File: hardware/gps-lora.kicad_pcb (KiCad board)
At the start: 4 copper layers, 0 parts

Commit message: Complete schematic, place and partially route the PCB
Schematic:
- Add Storage & Display sheet (microSD, FH12 OLED connector, TLV75801
  3.8 V VBAT regulator, charge-pump parts) and Radio sheet fixes
- Select remaining parts (PTS810, 1206L075THYR, SMF5.0A, MCP120 EN
  supervisor DNP, Elna DSK backup cap), add mounting holes and fiducials
- Pin changes for routability: PPS -> IO15, LoRa MOSI -> IO47,
  LoRa RESET -> IO48, LoRa DIO0 -> IO1
- Remove optional SPI clock filter parts (R309/C307, R310/C308)
- Remove company name from title blocks (personal project)

PCB (60 x 120 mm, 4 layers):
- Place all parts; GNSS zone with custom DRC rules (kicad_dru)
- Project ESP32-S3-WROOM-1 footprint with 0.4 mm thermal vias
- GND / +3V3 / +5V copper zones
- Route power path, GNSS, microSD and LoRa buses
- DRC clean except unrouted nets and expected silkscreen-at-edge items

Docs: selected-parts table, pin table and EMC deviation in PCB_DESIGN.md

Co-Authored-By: Claude Opus 5.5 <noreply@anthropic.com>
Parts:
- added C201: 4.7nF, Capacitor_SMD:C_0402_1005Metric, F.Cu at (78.8, 145.2)
- added C202: 2200uF, Capacitor_SMD:CP_Elec_10x10.5, F.Cu at (61.8, 118.5)
- added C203: 22uF, Capacitor_SMD:C_0805_2012Metric, F.Cu at (79.6, 141.0)
- added C204: 100nF, Capacitor_SMD:C_0402_1005Metric, F.Cu at (81.0, 143.0)
- added C205: 22uF, Capacitor_SMD:C_0805_2012Metric, F.Cu at (85.6, 141.0)
- added C206: 100nF, Capacitor_SMD:C_0402_1005Metric, F.Cu at (83.6, 143.0)
- added C301: 100uF, Capacitor_SMD:C_1210_3225Metric, F.Cu at (107.0, 123.4)
- added C302: 10uF, Capacitor_SMD:C_0805_2012Metric, F.Cu at (107.6, 126.6)
- added C303: 100nF, Capacitor_SMD:C_0402_1005Metric, F.Cu at (107.2, 128.8)
- added C304: 1uF, Capacitor_SMD:C_0402_1005Metric, F.Cu at (105.6, 128.8)
- added C305: DNP, Capacitor_SMD:C_0402_1005Metric, F.Cu at (92.0, 126.8)
- added C306: DNP, Capacitor_SMD:C_0402_1005Metric, F.Cu at (93.3, 126.8)
- added C401: 10uF, Capacitor_SMD:C_0805_2012Metric, F.Cu at (84.0, 50.2)
- added C402: 100nF, Capacitor_SMD:C_0402_1005Metric, F.Cu at (81.9, 50.9)
- added C404: 100uF, Capacitor_SMD:C_1210_3225Metric, F.Cu at (68.6, 109.2)
- added C405: 10uF, Capacitor_SMD:C_0805_2012Metric, F.Cu at (64.6, 108.6)
- added C406: 100nF, Capacitor_SMD:C_0402_1005Metric, F.Cu at (61.8, 108.4)
- added C501: 100uF, Capacitor_SMD:C_1210_3225Metric, F.Cu at (62.6, 126.2)
- added C502: 10uF, Capacitor_SMD:C_0805_2012Metric, F.Cu at (58.0, 128.4)
- added C503: 100nF, Capacitor_SMD:C_0402_1005Metric, F.Cu at (57.5, 130.9)
- added C504: 1uF, Capacitor_SMD:C_0402_1005Metric, F.Cu at (90.6, 126.3)
- added C505: 1uF, Capacitor_SMD:C_0402_1005Metric, F.Cu at (89.4, 126.3)
- added C506: 1uF, Capacitor_SMD:C_0402_1005Metric, F.Cu at (88.2, 126.3)
- added C507: 1uF, Capacitor_SMD:C_0402_1005Metric, F.Cu at (87.0, 126.3)
- added C508: 2.2uF, Capacitor_SMD:C_0603_1608Metric, F.Cu at (78.4, 126.3)
- added C509: 4.7uF, Capacitor_SMD:C_0603_1608Metric, F.Cu at (80.0, 126.3)
- added C510: 1uF, Capacitor_SMD:C_0402_1005Metric, F.Cu at (89.2, 129.0)
- added C511: 1uF, Capacitor_SMD:C_0402_1005Metric, F.Cu at (83.4, 129.1)
- added D201: SMF5.0A, Diode_SMD:D_SOD-123F, F.Cu at (75.5, 134.5)
- added D202: Schottky, Diode_SMD:D_SMA, F.Cu at (71.0, 130.6)
- added D301: Green, LED_SMD:LED_0603_1608Metric, F.Cu at (101.3, 126.3)
- added D401: BAT54, Diode_SMD:D_SOD-323, F.Cu at (71.5, 83.5)
- added F201: 0.75A PTC, Fuse:Fuse_1206_3216Metric, F.Cu at (75.5, 137.5)
- added FID1: Fiducial, Fiducial:Fiducial_1mm_Mask2mm, F.Cu at (72.0, 33.0)
- added FID2: Fiducial, Fiducial:Fiducial_1mm_Mask2mm, F.Cu at (107.0, 80.0)
- added FID3: Fiducial, Fiducial:Fiducial_1mm_Mask2mm, F.Cu at (53.0, 122.0)
- added H1: MountingHole_Pad, MountingHole:MountingHole_2.2mm_M2_Pad_Via, F.Cu at (53.5, 33.5)
- added H2: MountingHole_Pad, MountingHole:MountingHole_2.2mm_M2_Pad_Via, F.Cu at (106.5, 33.5)
- added H3: MountingHole_Pad, MountingHole:MountingHole_2.2mm_M2_Pad_Via, F.Cu at (53.5, 129.5)
- added H4: MountingHole_Pad, MountingHole:MountingHole_2.2mm_M2_Pad_Via, F.Cu at (82.5, 147.0)
- added J201: TYPE-C-31-M-12, Connector_USB:USB_C_Receptacle_HRO_TYPE-C-31-M-12, F.Cu at (72.4, 146.3)
- added J301: TC2030-NL, Connector:Tag-Connect_TC2030-IDC-NL_2x03_P1.27mm_Vertical, F.Cu at (101.5, 116.0)
- added J401: U.FL, Connector_Coaxial:U.FL_Hirose_U.FL-R-SMT-1_Vertical, F.Cu at (53.3, 110.0)
- added J501: DM3AT-SF-PEJM5, Connector_Card:microSD_HC_Hirose_DM3AT-SF-PEJM5, F.Cu at (59.0, 140.9)
- added J502: FH12-30S-0.5SH(55), Connector_FFC-FPC:Hirose_FH12-30S-0.5SH_1x30-1MP_P0.50mm_Horizontal, F.Cu at (86.5, 121.5)
- added R201: 5.1k, Resistor_SMD:R_0402_1005Metric, F.Cu at (69.0, 140.2)
- added R202: 5.1k, Resistor_SMD:R_0402_1005Metric, F.Cu at (75.0, 140.2)
- added R203: 1M, Resistor_SMD:R_0402_1005Metric, F.Cu at (78.8, 143.4)
- added R204: 0R, Resistor_SMD:R_0805_2012Metric, F.Cu at (76.3, 130.6)
- added R205: 10k, Resistor_SMD:R_0402_1005Metric, F.Cu at (100.6, 129.0)
- added R206: 15k, Resistor_SMD:R_0402_1005Metric, F.Cu at (101.9, 129.0)
- added R301: 10k, Resistor_SMD:R_0402_1005Metric, F.Cu at (104.4, 128.8)
- added R302: 10k, Resistor_SMD:R_0402_1005Metric, F.Cu at (94.6, 126.8)
- added R303: 1k, Resistor_SMD:R_0402_1005Metric, F.Cu at (99.7, 126.8)
- added R304: 0R, Resistor_SMD:R_0402_1005Metric, F.Cu at (92.0, 129.0)
- added R305: 0R, Resistor_SMD:R_0402_1005Metric, F.Cu at (93.3, 129.0)
- added R306: 499R, Resistor_SMD:R_0402_1005Metric, F.Cu at (99.0, 120.2)
- added R307: 100R, Resistor_SMD:R_0402_1005Metric, F.Cu at (97.1, 129.0)
- added R308: 100R, Resistor_SMD:R_0402_1005Metric, F.Cu at (95.8, 129.0)
- added R401: 1k, Resistor_SMD:R_0402_1005Metric, F.Cu at (71.5, 80.0)
- added R501: 47k, Resistor_SMD:R_0402_1005Metric, F.Cu at (59.5, 130.6)
- added R502: 47k, Resistor_SMD:R_0402_1005Metric, F.Cu at (60.8, 130.6)
- added R503: 47k, Resistor_SMD:R_0402_1005Metric, F.Cu at (62.1, 130.6)
- added R504: 47k, Resistor_SMD:R_0402_1005Metric, F.Cu at (63.4, 130.6)
- added R505: 10k, Resistor_SMD:R_0402_1005Metric, F.Cu at (85.8, 126.3)
- added R506: 4.7k, Resistor_SMD:R_0402_1005Metric, F.Cu at (84.6, 126.3)
- added R507: 4.7k, Resistor_SMD:R_0402_1005Metric, F.Cu at (83.4, 126.3)
- added R508: 390k, Resistor_SMD:R_0402_1005Metric, F.Cu at (81.6, 126.3)
- added R509: 59k, Resistor_SMD:R_0402_1005Metric, F.Cu at (82.2, 129.1)
- added R510: 10k, Resistor_SMD:R_0402_1005Metric, F.Cu at (81.0, 129.1)
- added SW301: RESET, Button_Switch_SMD:SW_SPST_PTS810, F.Cu at (106.5, 92.0)
- added SW302: BOOT, Button_Switch_SMD:SW_SPST_PTS810, F.Cu at (106.5, 99.0)
- added SW303: EJECT, Button_Switch_SMD:SW_SPST_PTS810, F.Cu at (106.5, 106.0)
- added TP201: TestPoint, TestPoint:TestPoint_Pad_D1.0mm, F.Cu at (68.5, 126.5)
- added TP202: TestPoint, TestPoint:TestPoint_Pad_D1.0mm, F.Cu at (71.0, 126.5)
- added TP203: TestPoint, TestPoint:TestPoint_Pad_D1.0mm, F.Cu at (73.5, 126.5)
- added TP204: TestPoint, TestPoint:TestPoint_Pad_D1.0mm, F.Cu at (76.0, 126.5)
- added TP401: SAFEBOOT, TestPoint:TestPoint_Pad_D1.0mm, F.Cu at (80.0, 79.6)
- added TP501: VBAT, TestPoint:TestPoint_Pad_D1.0mm, F.Cu at (79.4, 129.4)
- added U201: USBLC6-2SC6, Package_TO_SOT_SMD:SOT-23-6, F.Cu at (70.0, 137.5)
- added U202: AP7361C-33E, Package_TO_SOT_SMD:SOT-223-3_TabPin2, F.Cu at (82.5, 135.4)
- added U301: ESP32-S3-WROOM-1-N8, gps-lora:ESP32-S3-WROOM-1, F.Cu at (103.2, 140.0)
- added U302: MCP120T-300I/TT, Package_TO_SOT_SMD:SOT-23, F.Cu at (102.2, 122.0)
- added U401: SAM-M10Q, RF_GPS:ublox_SAM-M8Q, F.Cu at (80.0, 60.0)
- added U402: RFM95W-868S2, RF_Module:HOPERF_RFM9XW_SMD, F.Cu at (60.8, 98.0)
- added U501: TLV75801PDBV, Package_TO_SOT_SMD:SOT-23-5, F.Cu at (86.4, 129.1)
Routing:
- net GNSS_RESET_N: track 0.00 -> 107.6 mm, vias 0 -> 2
- net LORA_DIO0: track 0.00 -> 101.2 mm, vias 0 -> 4
- net +3V3: track 0.00 -> 99.6 mm, vias 0 -> 4
- net LORA_RESET: track 0.00 -> 86.9 mm, vias 0 -> 2
- net GNSS_PPS: track 0.00 -> 84.8 mm, vias 0 -> 2
- net LORA_DIO1: track 0.00 -> 83.4 mm, vias 0 -> 4
- net LORA_NSS: track 0.00 -> 82.3 mm, vias 0 -> 2
- net LORA_MOSI: track 0.00 -> 80.0 mm, vias 0 -> 2
- net GNSS_RXD: track 0.00 -> 77.9 mm, vias 0 -> 2
- net LORA_MISO: track 0.00 -> 77.2 mm, vias 0 -> 2
- net LORA_SCK: track 0.00 -> 77.0 mm, vias 0 -> 4
- net GNSS_TXD: track 0.00 -> 74.7 mm, vias 0 -> 2
- net SD_MISO: track 0.00 -> 57.8 mm, vias 0 -> 2
- net +5V: track 0.00 -> 56.9 mm, vias 0 -> 3
- net SD_CS: track 0.00 -> 43.7 mm, vias 0 -> 2
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- added copper zone on In2.Cu, net +3V3
- added copper zone on In2.Cu, net +5V
- added copper zone on B.Cu, net GND
- added copper zone on F.Cu, net GND
- added copper zone on In1.Cu, net GND
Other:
- board outline added: 60 x 120 mm
- board text added: "OLED PANEL - NO PARTS"

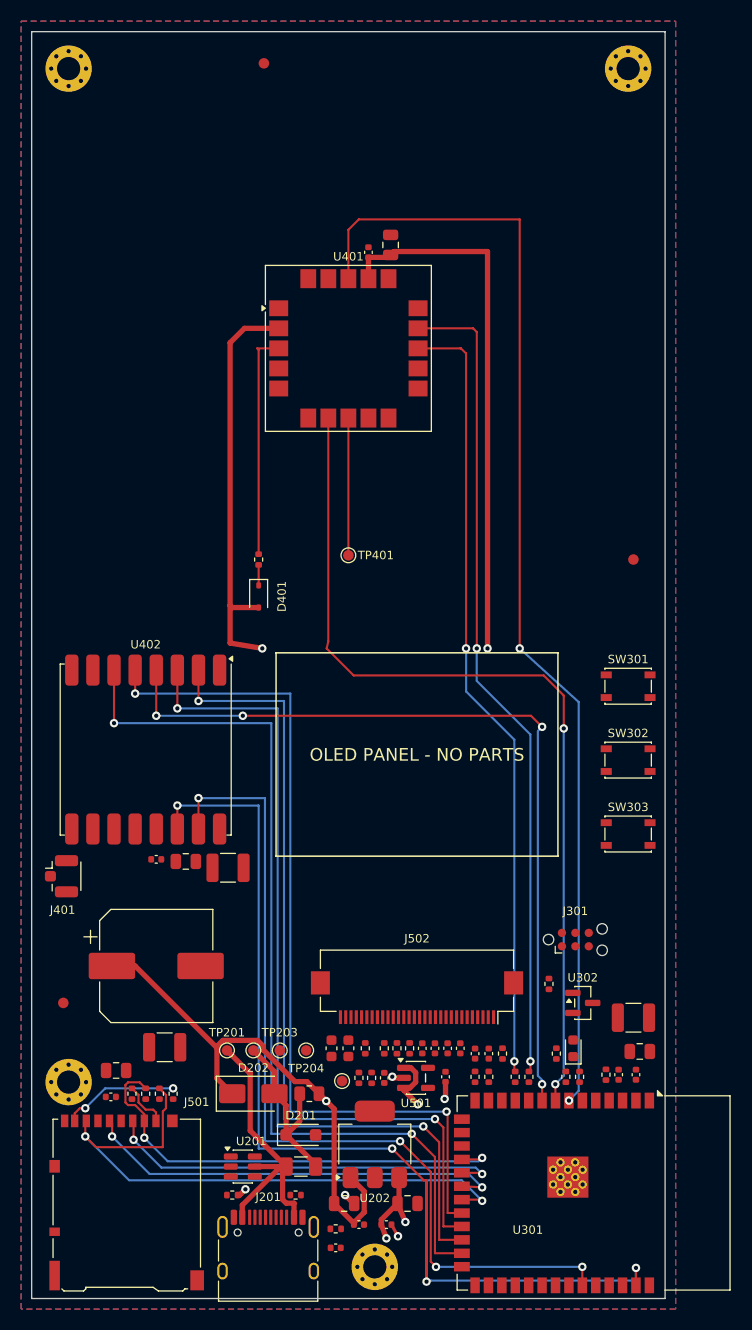
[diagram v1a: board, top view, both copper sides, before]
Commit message: Finish PCB routing, add BOM part numbers and fab export
Routing (DRC: 0 errors, 0 unconnected; ERC: 0)
- Complete the remaining nets on top of the GUI routing; GND stitching
  grid and edge fence; every GND pad reaches the L2 plane
- Re-lay the microSD bus under USB D+ so the USBLC6 and VBUS TVS get
  direct GND vias; lift LoRa NSS/MISO/MOSI to clear the TVS via
- Reroute D-, VBUS sense, CC2, BOOT, OLED SDA/SCL, LED and TXD0_R; remove
  vias in pads (R205, R505, R204, R507, U301 pin 7)
- Placement tweaks: C306 moved, C508/C509/R508 rotated 180, R302 moved
- PCB title block with rev v0.1

Parts and outputs
- MPN and Manufacturer fields on all placed parts (tools/add-mpn.py)
- tools/fab-export.py: ERC/DRC gate, zone refill, Gerbers, drill, BOM,
  pick-and-place and fab notes for Lion Circuits
- OLED panel DS501: schematic symbol and board-only 3D footprint
- Elna DSK footprint for C403 (not placed yet)
- kicad-routing skill under .claude/skills

Open before fab (see docs/PCB_DESIGN.md Open items): J502 pin order is
mirrored against the panel FPC; Lion stackup widths; C403 placement.

Co-Authored-By: Claude Opus 5.5 <noreply@anthropic.com>
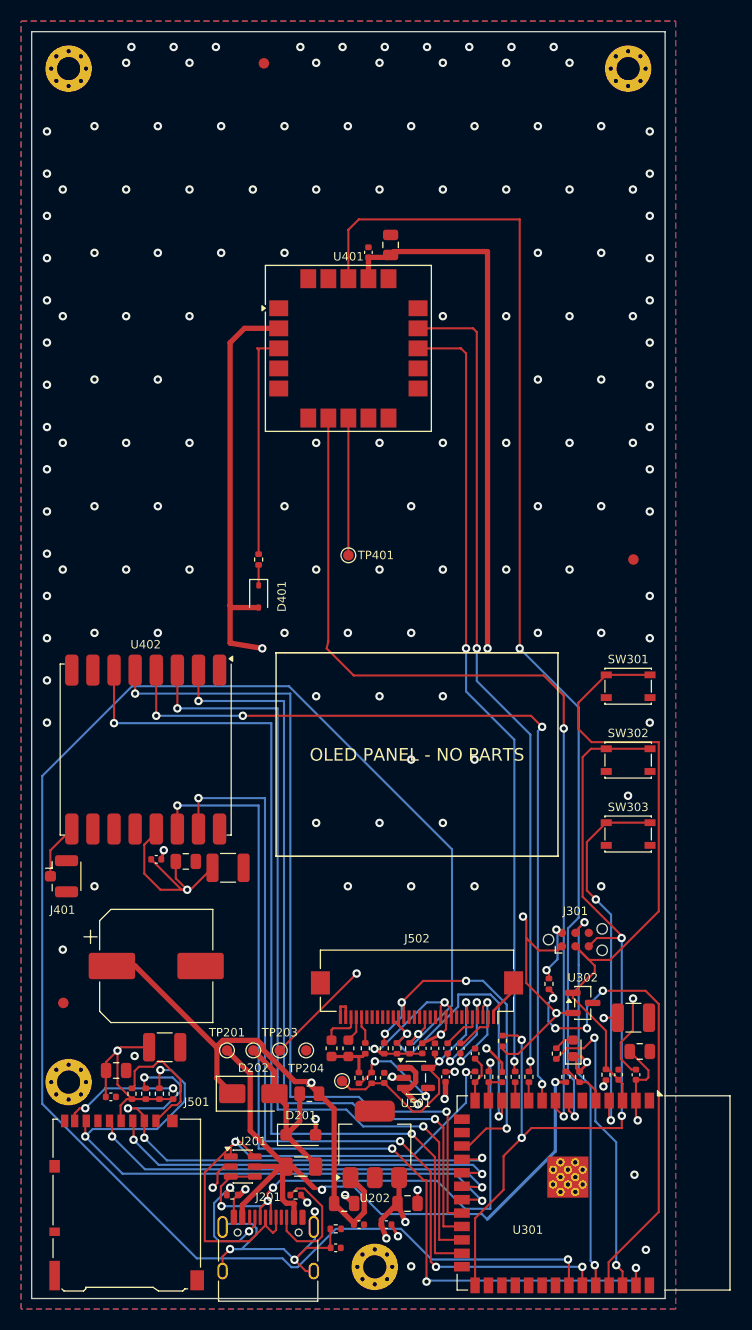
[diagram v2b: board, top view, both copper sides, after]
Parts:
- added DS501: ER-OLED0.96-1.1W, OLED_ER-OLED0.96-1.1W, F.Cu at (86.5, 98.5)
- moved C306 2.56 mm to (94.5, 129.0)
- moved R302 1.20 mm to (94.6, 125.6)
- turned C508 to -90 degrees
- turned C509 to -90 degrees
- turned R508 to -90 degrees
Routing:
- net OLED_RES: track 0.00 -> 165.7 mm, vias 0 -> 2
- net +3V3: track 99.6 -> 201.2 mm, vias 4 -> 14
- net /MCU/BOOT: track 0.00 -> 83.7 mm, vias 0 -> 4
- net /MCU/EN: track 0.00 -> 63.2 mm
- net USB_DP: track 0.00 -> 53.8 mm, vias 0 -> 2
- net USB_DN: track 0.00 -> 51.8 mm, vias 0 -> 4
- net /MCU/TXD0_R: track 0.00 -> 45.9 mm, vias 0 -> 4
- net GND: track 4.56 -> 44.5 mm, vias 4 -> 144
- net VBUS: track 28.9 -> 66.9 mm, vias 0 -> 2
- net /MCU/UART0_RX: track 0.00 -> 36.6 mm, vias 0 -> 2
- net /MCU/EJECT: track 0.00 -> 36.0 mm, vias 0 -> 2
- net OLED_SCL: track 0.00 -> 34.4 mm, vias 0 -> 4
- net OLED_SDA: track 0.00 -> 32.5 mm, vias 0 -> 2
- net Net-(J201-SHIELD): track 0.00 -> 30.9 mm, vias 0 -> 3
- net /MCU/LED: track 0.00 -> 29.0 mm, vias 0 -> 2
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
